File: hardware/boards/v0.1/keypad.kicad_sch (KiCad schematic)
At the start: 70 parts, among them SW1 TRIG1, SW10 TRIG10, SW11 TRIG11, SW12 TRIG12, SW13 TRIG13, SW14 TRIG14, SW15 TRIG15, SW16 TRIG16, SW18 HELP, SW2 TRIG2, SW3 TRIG3, SW4 TRIG4, SW5 TRIG5, SW6 TRIG6, SW7 TRIG7, SW8 TRIG8, SW9 TRIG9, U25 TCA8418RTWR

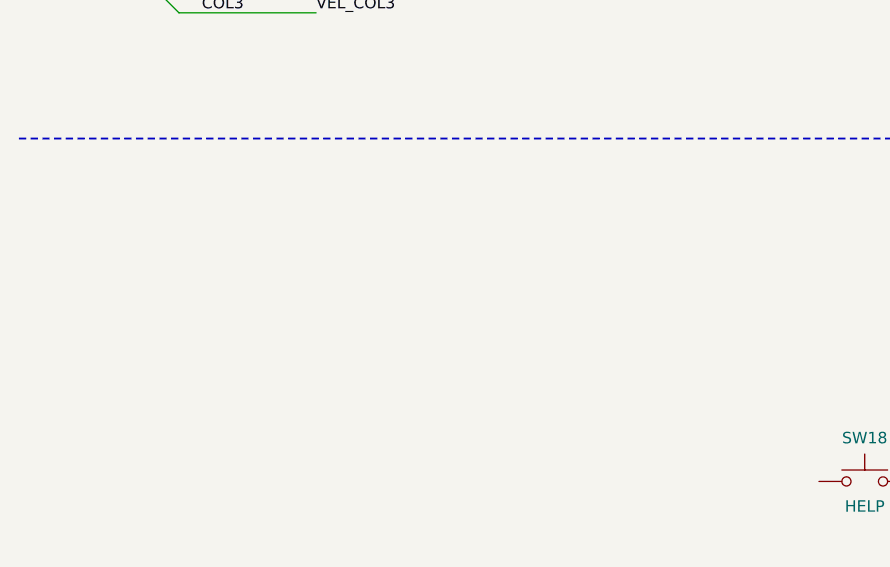
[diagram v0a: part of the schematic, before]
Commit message: feat: various component and layout changes
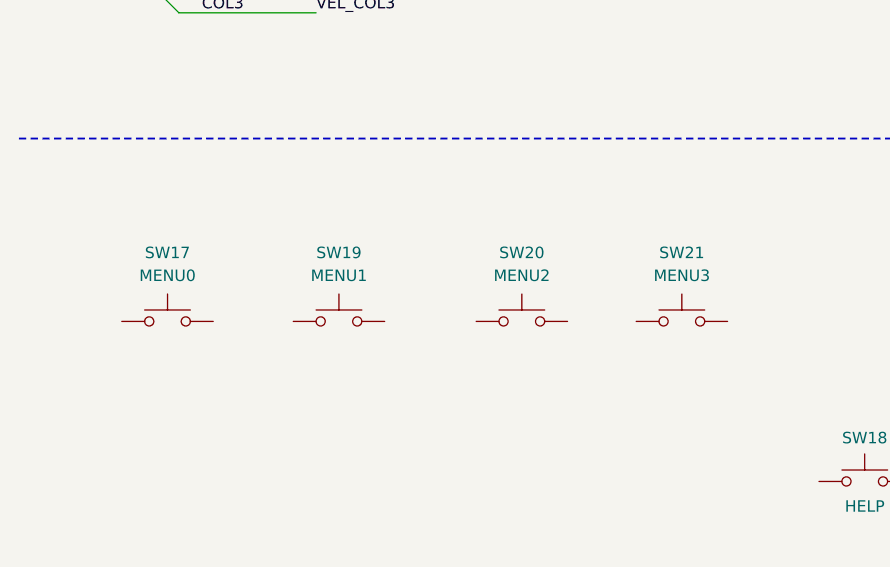
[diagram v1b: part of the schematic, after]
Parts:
- added SW17: MENU0, Button_Switch_SMD:SW_SPST_B3S-1000, symbol Switch:SW_Push
- added SW19: MENU1, Button_Switch_SMD:SW_SPST_B3S-1000, symbol Switch:SW_Push
- added SW20: MENU2, Button_Switch_SMD:SW_SPST_B3S-1000, symbol Switch:SW_Push
- added SW21: MENU3, Button_Switch_SMD:SW_SPST_B3S-1000, symbol Switch:SW_Push

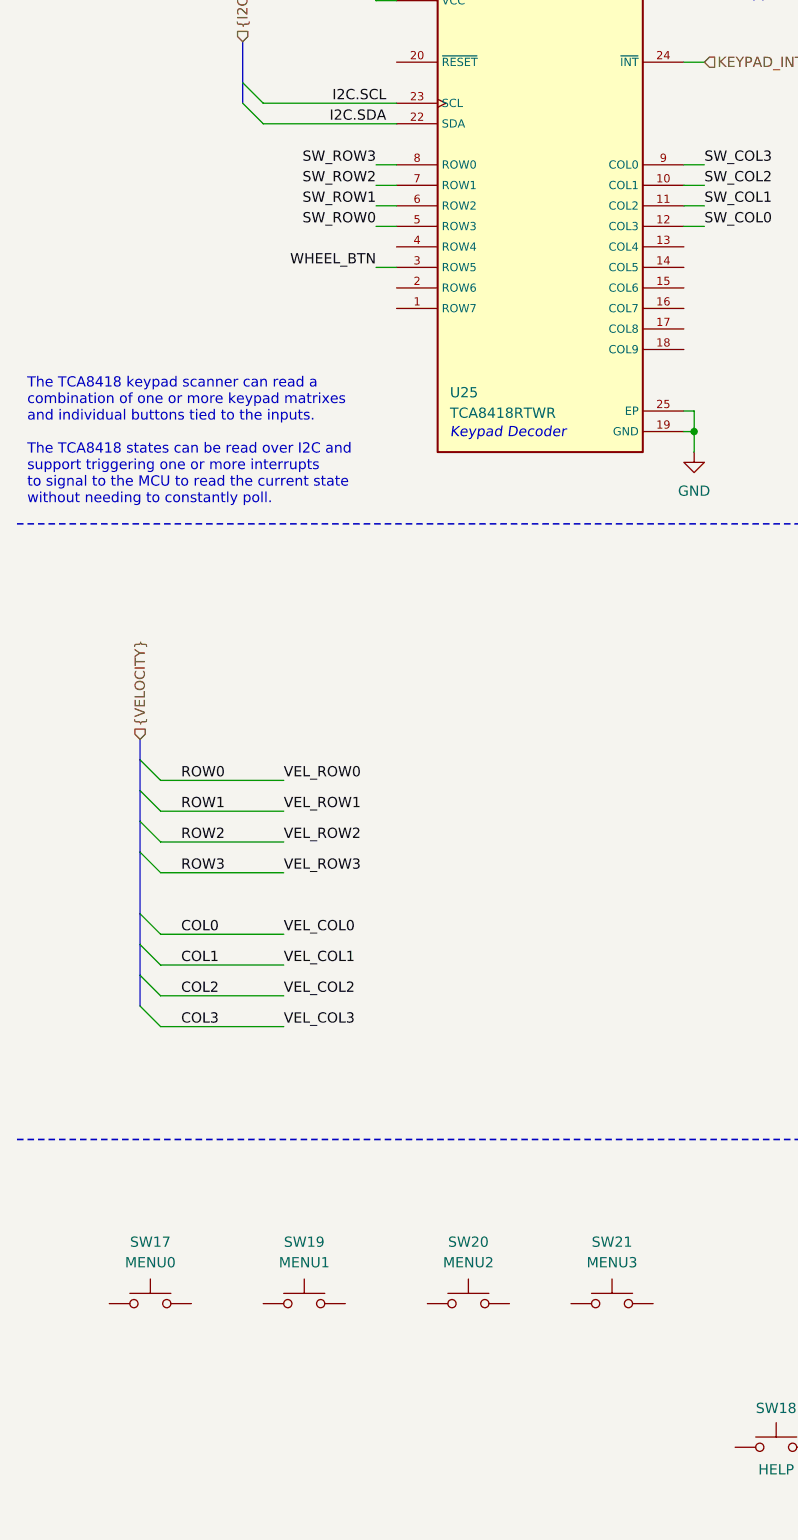
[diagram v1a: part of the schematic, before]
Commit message: feat: start MIDI and CV schematic
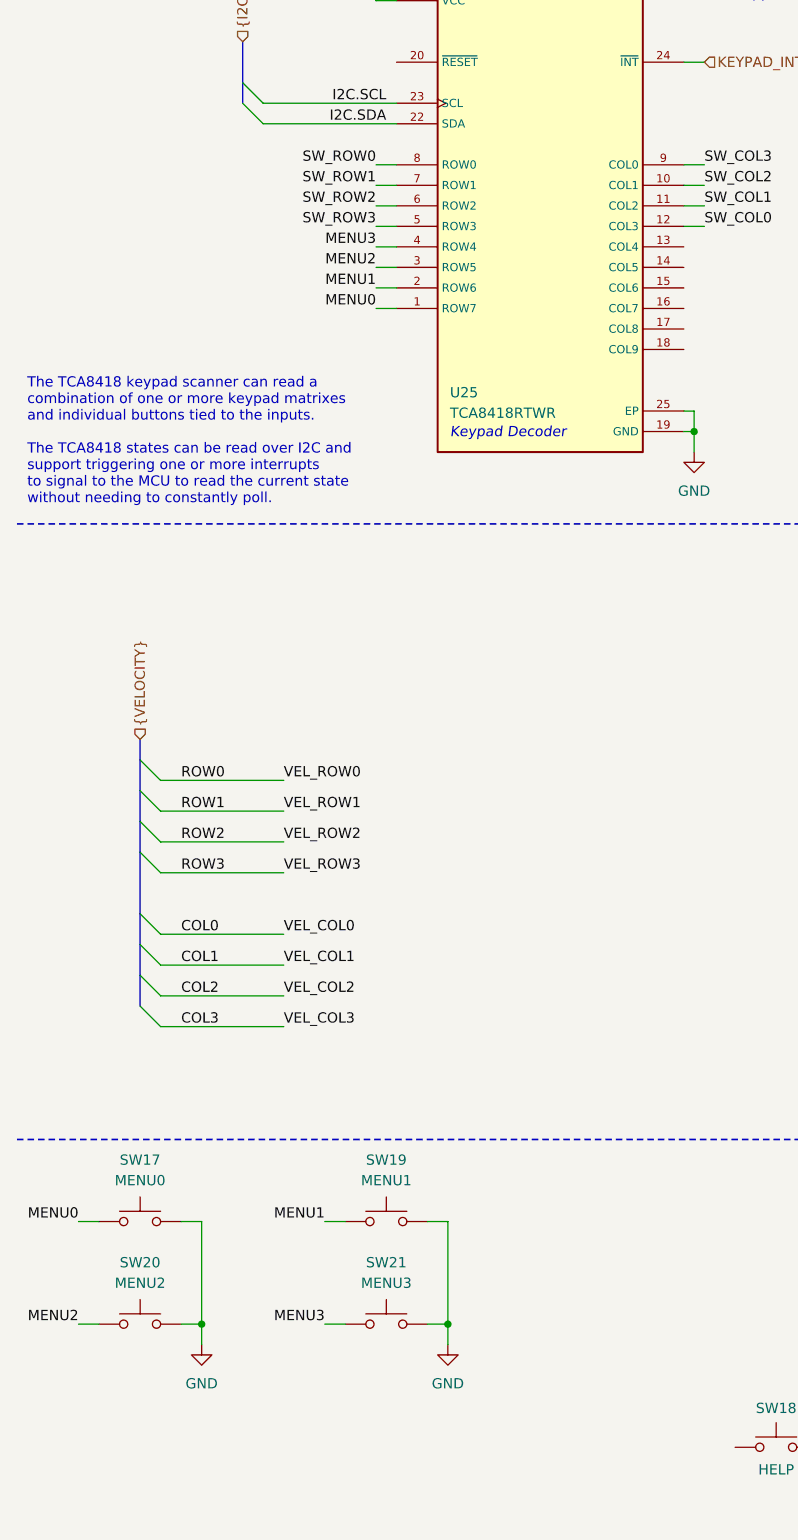
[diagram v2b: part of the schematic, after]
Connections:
- net WHEEL_BTN is gone; now on net MENU2: U25.3 (ROW5)
- net GND: now also SW17.2, SW19.2, SW20.2, SW21.2
- net SW_ROW0: now also U25.8 (ROW0); no longer U25.5 (ROW3)
- net SW_ROW1: now also U25.7 (ROW1); no longer U25.6 (ROW2)
- net SW_ROW2: now also U25.6 (ROW2); no longer U25.7 (ROW1)
- net SW_ROW3: now also U25.5 (ROW3); no longer U25.8 (ROW0)
- net MENU0: now reaches U25.1 (ROW7)
- net MENU0: now also SW17.1
- net MENU1: now reaches U25.2 (ROW6)
- net MENU1: now also SW19.1
- net MENU3: now reaches U25.4 (ROW4)
- net MENU3: now also SW21.1
- net MENU2: now reaches SW20.1
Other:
- moved on the sheet: SW17, SW19, SW20, SW21

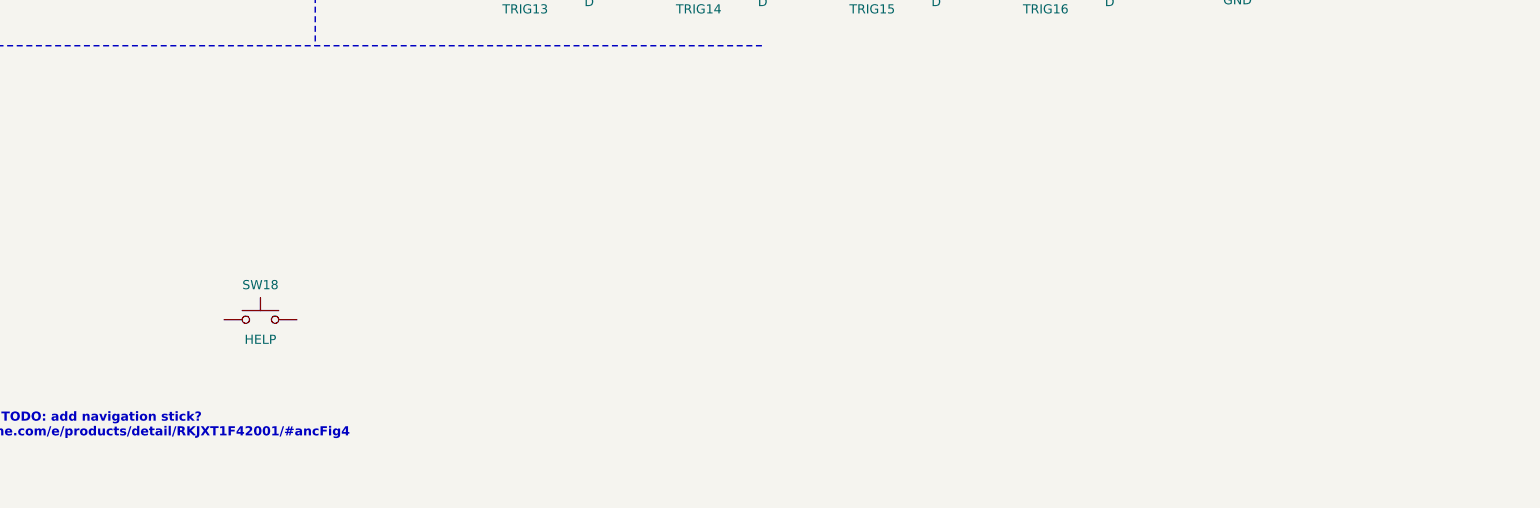
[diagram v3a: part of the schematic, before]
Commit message: fix: I2C routing for keypad
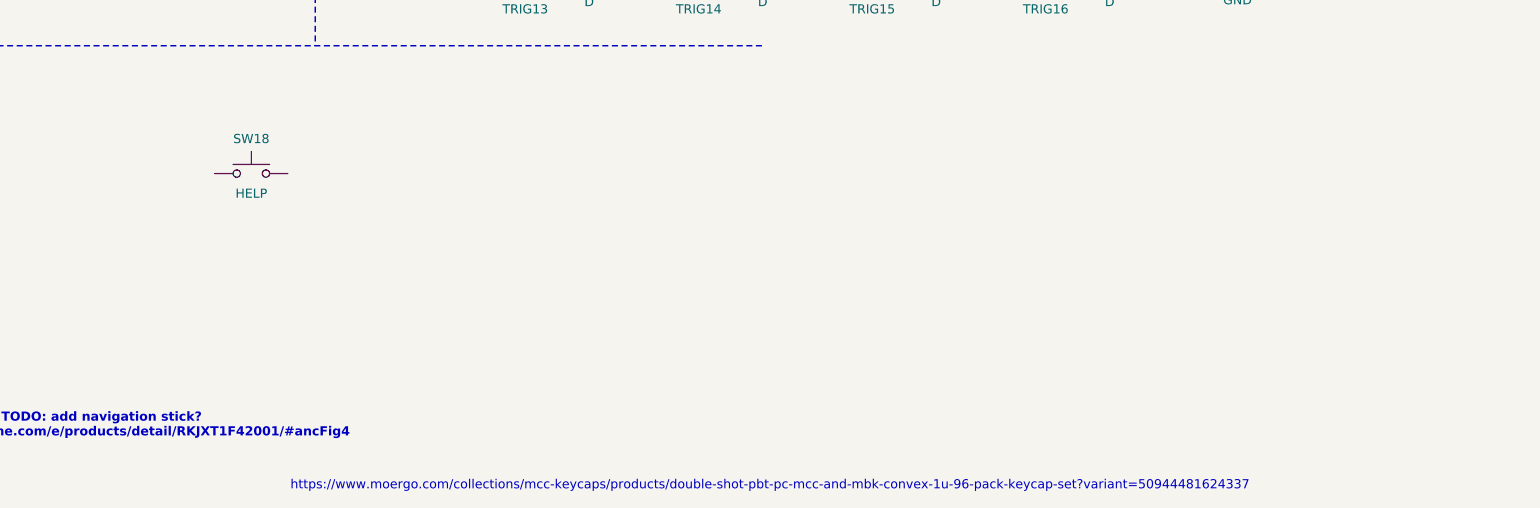
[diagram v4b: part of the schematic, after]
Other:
- note added: "https://www.moergo.com/collections/mcc-keycaps/products/double-shot-pbt-pc-mcc-and-mbk-convex-1u-96-pack-keycap-set?variant=50944481624337"
- moved on the sheet: SW18
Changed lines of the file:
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@@
 		)
 	)
+	(text "https://www.moergo.com/collections/mcc-keycaps/products/double-shot-pbt-pc-mcc-and-mbk-convex-1u-96-pack-keycap-set?variant=50944481624337"
+		(exclude_from_sim no)
+		(at 177.546 227.584 0)
+		(effects
+			(font
+				(size 1.27 1.27)
+			)
+		)
+	)
 	(text "The TCA8418 keypad scanner can read a\ncombination of one or more keypad matrixes\nand individual buttons tied to the inputs.\n\nThe TCA8418 states can be read over I2C and\nsupport triggering one or more interrupts\nto signal to the MCU to read the current state\nwithout needing to constantly poll."
 		(exclude_from_sim no)
@@
 	(symbol
 		(lib_id "Switch:SW_Push")
-		(at 106.68 204.47 0)
+		(at 105.41 184.15 0)
 		(unit 1)
 		(exclude_from_sim no)
@@
 		(dnp no)
 		(property "Reference" "SW18"
-			(at 106.68 199.644 0)
+			(at 105.41 179.324 0)
 			(effects
 				(font
@@
 		)
 		(property "Value" "HELP"
-			(at 106.68 206.502 0)
+			(at 105.41 186.182 0)
 			(effects
 				(font
@@
 		)
 		(property "Footprint" "Button_Switch_SMD:SW_SPST_EVQQ2"
-			(at 106.68 199.39 0)
+			(at 105.41 179.07 0)
 			(effects
 				(font
@@
 		)
 		(property "Datasheet" "~"
-			(at 106.68 199.39 0)
+			(at 105.41 179.07 0)
 			(effects
 				(font
@@
 		)
 		(property "Description" "Push button switch, generic, two pins"
-			(at 106.68 204.47 0)
+			(at 105.41 184.15 0)
 			(effects
 				(font
@@
 		)
 		(property "JLC" ""
-			(at 106.68 204.47 0)
+			(at 105.41 184.15 0)
 			(effects
 				(font
@@
 		)
 		(property "Arrow Part Number" ""
-			(at 106.68 204.47 0)
+			(at 105.41 184.15 0)
 			(effects
 				(font
@@
 		)
 		(property "Arrow Price/Stock" ""
-			(at 106.68 204.47 0)
+			(at 105.41 184.15 0)
 			(effects
 				(font
@@
 		)
 		(property "MANUFACTURER" ""
-			(at 106.68 204.47 0)
+			(at 105.41 184.15 0)
 			(effects
 				(font
@@
 		)
 		(property "MAXIMUM_PACKAGE_HEIGHT" ""
-			(at 106.68 204.47 0)
+			(at 105.41 184.15 0)
 			(effects
 				(font
@@
 		)
 		(property "PARTREV" ""
-			(at 106.68 204.47 0)
+			(at 105.41 184.15 0)
 			(effects
 				(font
@@
 		)
 		(property "STANDARD" ""
-			(at 106.68 204.47 0)
+			(at 105.41 184.15 0)
 			(effects
 				(font
@@
 		)
 		(property "Connector" ""
-			(at 106.68 204.47 0)
+			(at 105.41 184.15 0)
 			(effects
 				(font

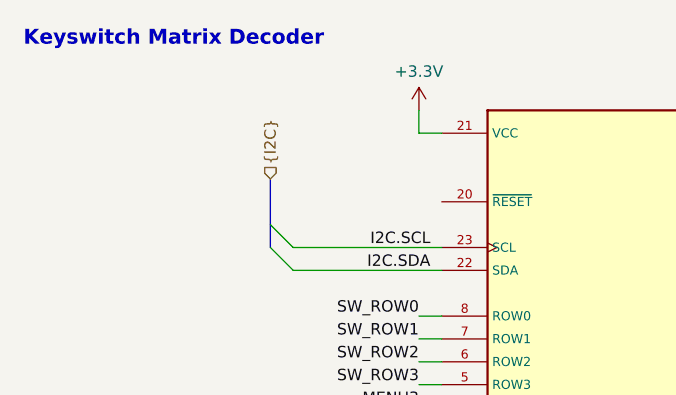
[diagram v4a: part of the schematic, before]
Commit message: feat: schematic organization and ERC cleanup
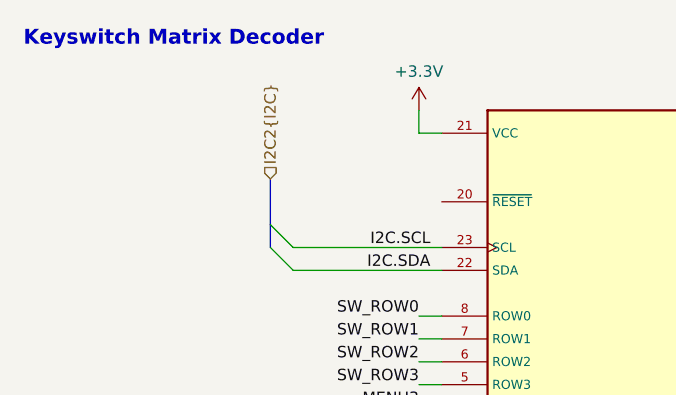
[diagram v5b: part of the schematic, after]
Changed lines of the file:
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@@
 		)
 	)
-	(hierarchical_label "{I2C}"
+	(hierarchical_label "I2C2{I2C}"
 		(shape input)
 		(at 40.64 30.48 90)

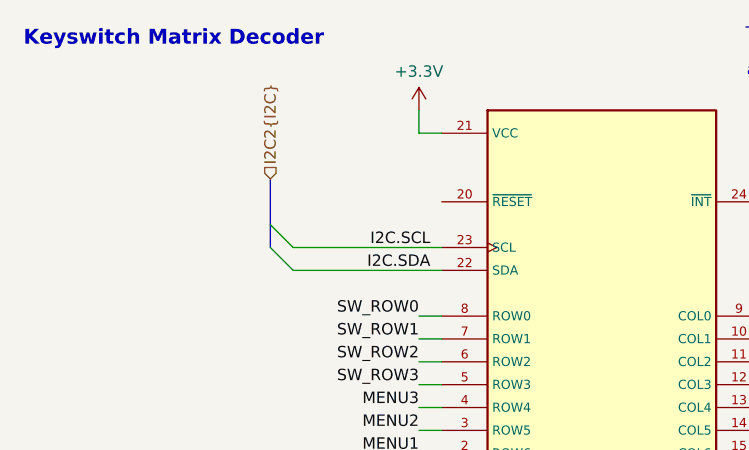
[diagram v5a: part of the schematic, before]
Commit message: feat: add touch screen connector, input I2C bus
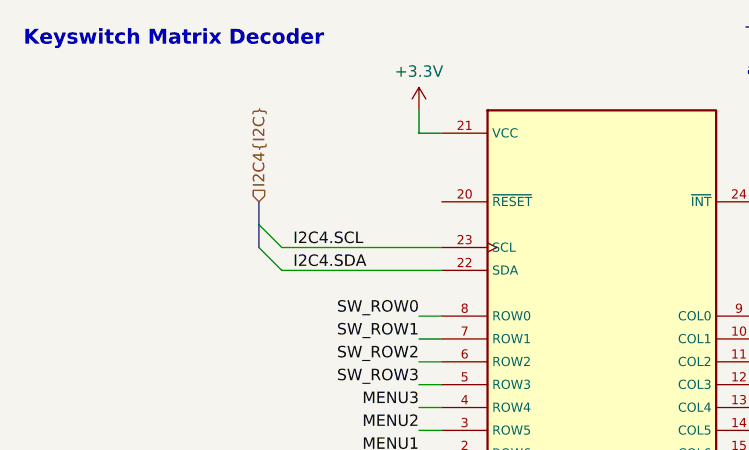
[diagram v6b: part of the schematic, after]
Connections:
- net I2C.SCL renamed I2C4.SCL
- net I2C.SDA renamed I2C4.SDA
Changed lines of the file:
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@@
 	)
 	(bus_entry
-		(at 43.18 40.64)
+		(at 30.48 133.35)
 		(size -2.54 -2.54)
 		(stroke
@@
 	)
 	(bus_entry
-		(at 30.48 133.35)
+		(at 30.48 144.78)
 		(size -2.54 -2.54)
 		(stroke
@@
 	)
 	(bus_entry
-		(at 30.48 144.78)
+		(at 41.91 38.1)
 		(size -2.54 -2.54)
 		(stroke
@@
 	)
 	(bus_entry
-		(at 30.48 125.73)
+		(at 41.91 40.64)
 		(size -2.54 -2.54)
 		(stroke
@@
 	)
 	(bus_entry
-		(at 30.48 148.59)
+		(at 30.48 125.73)
 		(size -2.54 -2.54)
 		(stroke
@@
 	)
 	(bus_entry
-		(at 43.18 38.1)
+		(at 30.48 148.59)
 		(size -2.54 -2.54)
 		(stroke
@@
 		)
 	)
-	(bus
-		(pts
-			(xy 40.64 30.48) (xy 40.64 35.56)
-		)
-		(stroke
-			(width 0)
-			(type default)
-		)
-	)
 	(wire
 		(pts
@@
 	(bus
 		(pts
-			(xy 27.94 127) (xy 27.94 130.81)
+			(xy 39.37 35.56) (xy 39.37 38.1)
 		)
 		(stroke
@@
 		)
 	)
-	(wire
+	(bus
 		(pts
-			(xy 242.57 119.38) (xy 240.03 119.38)
+			(xy 27.94 127) (xy 27.94 130.81)
 		)
 		(stroke
@@
 	(wire
 		(pts
-			(xy 210.82 142.24) (xy 212.09 142.24)
+			(xy 242.57 119.38) (xy 240.03 119.38)
 		)
 		(stroke
@@
 	(wire
 		(pts
-			(xy 132.08 43.18) (xy 135.89 43.18)
+			(xy 210.82 142.24) (xy 212.09 142.24)
 		)
 		(stroke
@@
 		)
 	)
-	(bus
+	(wire
 		(pts
-			(xy 40.64 35.56) (xy 40.64 38.1)
+			(xy 132.08 43.18) (xy 135.89 43.18)
 		)
 		(stroke
@@
 	(wire
 		(pts
-			(xy 43.18 40.64) (xy 59.69 40.64)
+			(xy 57.15 63.5) (xy 59.69 63.5)
 		)
 		(stroke
@@
 		)
 	)
-	(wire
+	(bus
 		(pts
-			(xy 57.15 63.5) (xy 59.69 63.5)
+			(xy 39.37 33.02) (xy 39.37 35.56)
 		)
 		(stroke
@@
 	(wire
 		(pts
+			(xy 41.91 40.64) (xy 59.69 40.64)
+		)
+		(stroke
+			(width 0)
+			(type default)
+		)
+	)
+	(wire
+		(pts
 			(xy 187.96 50.8) (xy 186.69 50.8)
 		)
@@
 	(wire
 		(pts
+			(xy 41.91 38.1) (xy 59.69 38.1)
+		)
+		(stroke
+			(width 0)
+			(type default)
+		)
+	)
+	(wire
+		(pts
 			(xy 180.34 111.76) (xy 181.61 111.76)
 		)
@@
 	(wire
 		(pts
-			(xy 43.18 38.1) (xy 59.69 38.1)
-		)
-		(stroke
-			(width 0)
-			(type default)
-		)
-	)
-	(wire
-		(pts
 			(xy 161.29 73.66) (xy 186.69 73.66)
 		)
@@
 		)
 	)
-	(label "I2C.SCL"
-		(at 58.42 38.1 180)
-		(effects
-			(font
-				(size 1.27 1.27)
-			)
-			(justify right bottom)
-		)
-	)
 	(label "MENU2"
 		(at 57.15 58.42 180)
@@
 		)
 	)
-	(label "I2C.SDA"
-		(at 58.42 40.64 180)
-		(effects
-			(font
-				(size 1.27 1.27)
-			)
-			(justify right bottom)
-		)
-	)
 	(label "SW_COL0"
 		(at 97.79 53.34 0)
@@
 		)
 	)
+	(label "I2C4.SDA"
+		(at 43.18 40.64 0)
+		(effects
+			(font
+				(size 1.27 1.27)
+			)
+			(justify left bottom)
+		)
+	)
 	(label "MENU0"
 		(at 57.15 63.5 180)
@@
 		)
 	)
+	(label "I2C4.SCL"
+		(at 43.18 38.1 0)
+		(effects
+			(font
+				(size 1.27 1.27)
+			)
+			(justify left bottom)
+		)
+	)
 	(label "MENU3"
 		(at 57.15 55.88 180)
@@
 		)
 	)
-	(hierarchical_label "KEYPAD_INT"
+	(hierarchical_label "I2C4{I2C}"
 		(shape input)
-		(at 97.79 33.02 0)
+		(at 39.37 33.02 90)
 		(effects
 			(font
@@
 		)
 	)
-	(hierarchical_label "I2C2{I2C}"
+	(hierarchical_label "KEYPAD_INT"
 		(shape input)
-		(at 40.64 30.48 90)
+		(at 97.79 33.02 0)
 		(effects
 			(font
